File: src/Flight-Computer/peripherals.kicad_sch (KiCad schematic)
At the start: 0 parts

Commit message: implemented usb transceiver in schematic
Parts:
- added C16: 1uF, symbol Flight-Computer:CAP_0603
- added C17: 0.1uF, symbol Flight-Computer:CAP_0603
- added D6: SP0504BAHTG, SOD-123FL_MCC, symbol Flight-Computer:SP0504BAHTG
- added P3: USB, BEL_SS-52300-001, symbol Flight-Computer:USB
- added R3: 4.7k, symbol Flight-Computer:RES_0603
- added R5: 10k, symbol Flight-Computer:RES_0603
- added U3: CP2102-GMR(QFN28), QFN28G_0.5-5X5MM, symbol Flight-Computer:CP2102-GMR(QFN28)
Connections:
- new net 3.3V: R3.1
- new net 5V: C16.1, C17.1, D6.1, P3.1 (VCC), U3.7 (REGIN), U3.8 (VBUS)
- new net D+: D6.4, P3.3 (D+), U3.4 (D+)
- new net D-: D6.3, P3.2 (D-), U3.5 (D-)
- new net Earth: C16.2, C17.2, D6.2, P3.5 (GND), P3.S1 (SHIELD), P3.S2 (SHIELD), R5.1, U3.29 (PAD), U3.3 (GND)
- new net RX_USB: U3.25 (RXD)
- new net TX_USB: U3.26 (TXD)
- new net ~{USB_RST}: R3.2, U3.9 (~{RST})
- new net ~{USB_SUSPEND}: R5.2, U3.11 (~{SUSPEND})
- no-connect marks 0 -> 20
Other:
- note added: "USB Transceiver"

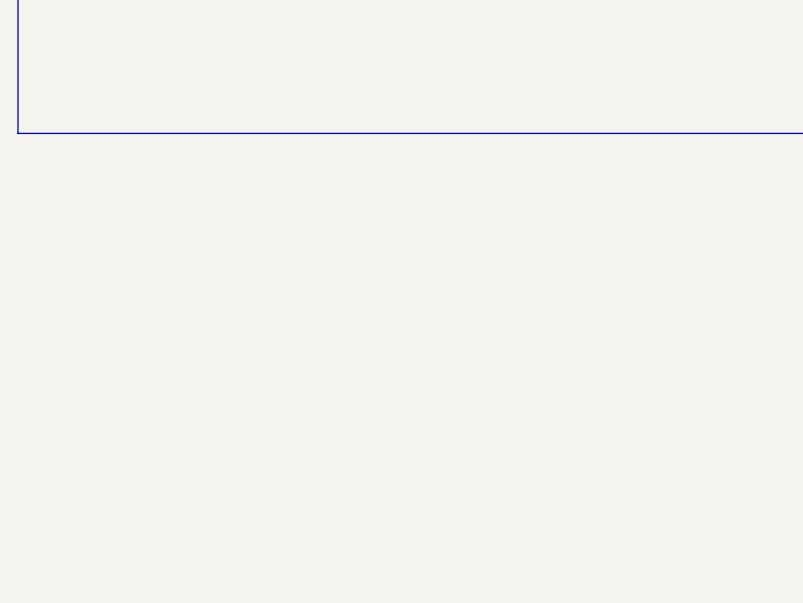
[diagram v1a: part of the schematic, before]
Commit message: implemented flash in schematic
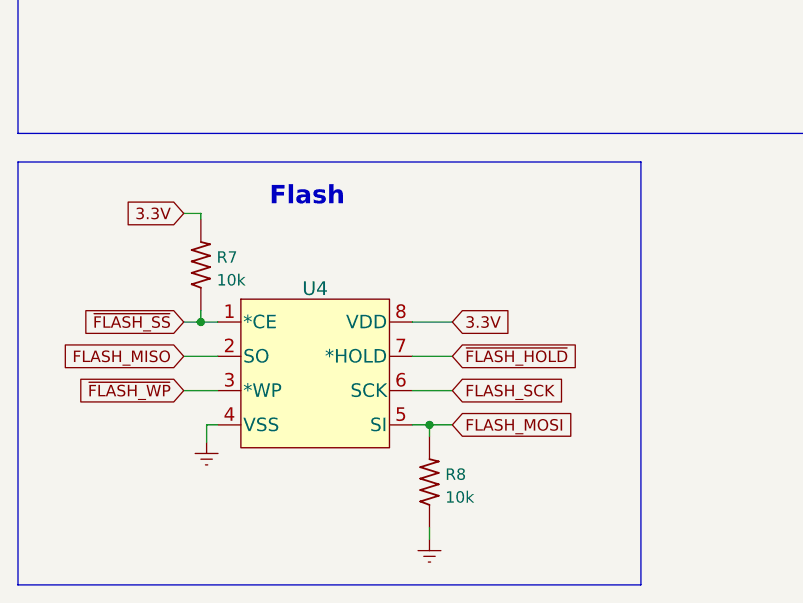
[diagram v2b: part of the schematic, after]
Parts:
- added R7, R8: 10k, symbol Flight-Computer:RES_0603
- added U4: SST25VF040B-50-4I-S2AE-T, SOIC8_S2A_SST_MCH, symbol Flight-Computer:SST25VF040B-50-4I-S2AE-T
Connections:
- net 3.3V: now also R7.2, U4.8 (VDD)
- net Earth: now also R8.1, U4.4 (VSS)
- new net FLASH_MISO: U4.2 (SO)
- new net FLASH_MOSI: R8.2, U4.5 (SI)
- new net FLASH_SCK: U4.6 (SCK)
- new net ~{FLASH_HOLD}: U4.7 (*HOLD)
- new net ~{FLASH_SS}: R7.1, U4.1 (*CE)
- new net ~{FLASH_WP}: U4.3 (*WP)
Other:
- note added: "Flash"

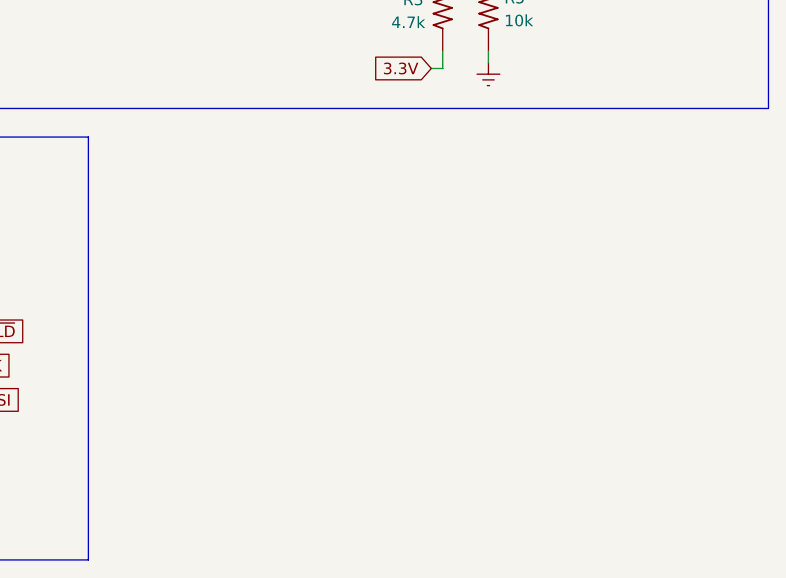
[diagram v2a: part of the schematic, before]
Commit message: added comparator to lib files
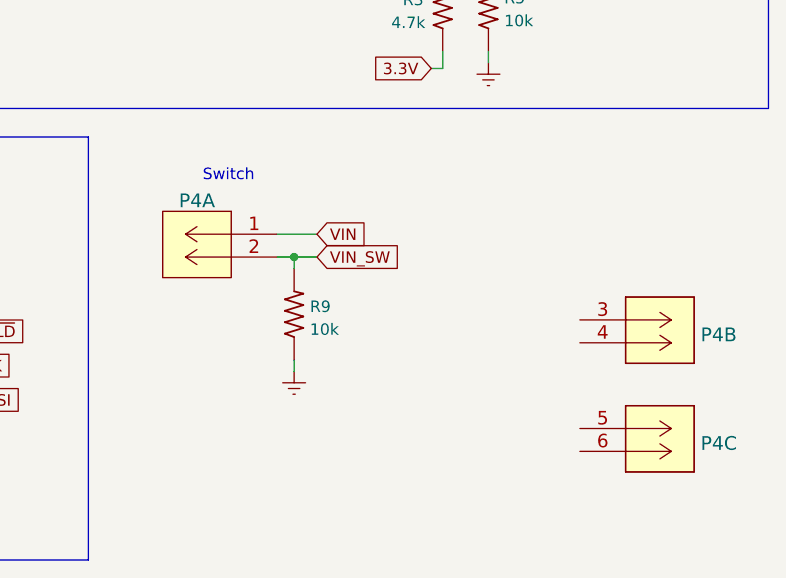
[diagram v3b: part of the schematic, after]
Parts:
- added P4: 282837-6, 66953-005LF_AMP, symbol Flight-Computer:282837-6
- added R9: 10k, symbol Flight-Computer:RES_0603
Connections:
- net Earth: now also R9.1
- new net VIN: P4.1 (5)
- new net VIN_SW: P4.2 (6), R9.2
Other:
- note added: "Switch"
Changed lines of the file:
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@@
   (junction (at 69.85 50.8) (diameter 0) (color 0 0 0 0)
+  )
+  (junction (at 109.855 107.95) (diameter 0) (color 0 0 0 0)
   )
   (junction (at 63.5 123.825) (diameter 0) (color 0 0 0 0)
@@
     (stroke (width 0) (type default) (color 0 0 0 0))
   )
+  (wire (pts (xy 107.95 107.95) (xy 109.855 107.95))
+    (stroke (width 0) (type default) (color 0 0 0 0))
+  )
   (wire (pts (xy 111.125 45.72) (xy 107.95 45.72))
     (stroke (width 0) (type default) (color 0 0 0 0))
@@
     (stroke (width 0) (type default) (color 0 0 0 0))
   )
+  (wire (pts (xy 109.855 107.95) (xy 112.395 107.95))
+    (stroke (width 0) (type default) (color 0 0 0 0))
+  )
   (wire (pts (xy 61.595 112.395) (xy 66.04 112.395))
     (stroke (width 0) (type default) (color 0 0 0 0))
@@
     (stroke (width 0) (type default) (color 0 0 0 0))
   )
+  (wire (pts (xy 109.855 107.95) (xy 109.855 109.22))
+    (stroke (width 0) (type default) (color 0 0 0 0))
+  )
   (wire (pts (xy 107.95 45.72) (xy 107.95 52.07))
     (stroke (width 0) (type default) (color 0 0 0 0))
@@
     (stroke (width 0) (type default) (color 0 0 0 0))
   )
+  (wire (pts (xy 109.855 119.38) (xy 109.855 120.65))
+    (stroke (width 0) (type default) (color 0 0 0 0))
+  )
   (polyline (pts (xy 17.78 18.415) (xy 17.78 91.44))
     (stroke (width 0) (type default) (color 0 0 0 0))
@@
     (stroke (width 0) (type default) (color 0 0 0 0))
   )
+  (wire (pts (xy 107.95 105.41) (xy 112.395 105.41))
+    (stroke (width 0) (type default) (color 0 0 0 0))
+  )
   (wire (pts (xy 61.595 123.825) (xy 63.5 123.825))
     (stroke (width 0) (type default) (color 0 0 0 0))
@@
   (wire (pts (xy 62.865 48.26) (xy 62.865 52.07))
     (stroke (width 0) (type default) (color 0 0 0 0))
+  )
+  (text "Switch" (at 99.695 99.695 0)
+    (effects (font (size 1.27 1.27)) (justify left bottom))
   )
   (text "Flash" (at 45.72 99.695 0)
@@
     )
   )
+  (global_label "VIN_SW" (shape input) (at 112.395 107.95 0) (fields_autoplaced)
+    (effects (font (size 1.27 1.27)) (justify left))
+    (property "Intersheet References" "${INTERSHEET_REFS}" (id 0) (at 121.3716 107.8706 0)
+      (effects (font (size 1.27 1.27)) (justify left) hide)
+    )
+  )
   (global_label "5V" (shape input) (at 121.285 69.215 180) (fields_autoplaced)
     (effects (font (size 1.27 1.27)) (justify right))
@@
     )
   )
+  (global_label "VIN" (shape input) (at 112.395 105.41 0) (fields_autoplaced)
+    (effects (font (size 1.27 1.27)) (justify left))
+    (property "Intersheet References" "${INTERSHEET_REFS}" (id 0) (at 117.743 105.3306 0)
+      (effects (font (size 1.27 1.27)) (justify left) hide)
+    )
+  )
   (global_label "3.3V" (shape input) (at 125.095 86.995 180) (fields_autoplaced)
     (effects (font (size 1.27 1.27)) (justify right))
@@
     )
   )
+  (symbol (lib_id "Flight-Computer:282837-6") (at 107.95 105.41 0) (mirror y) (unit 1)
+    (in_bom yes) (on_board yes) (fields_autoplaced)
+    (property "Reference" "P4" (id 0) (at 99.06 101.7031 0)
+      (effects (font (size 1.524 1.524)))
+    )
+    (property "Value" "282837-6" (id 1) (at 102.87 133.35 0)
+      (effects (font (size 1.524 1.524)) hide)
+    )
+    (property "Footprint" "66953-005LF_AMP" (id 2) (at 104.14 135.89 0)
+      (effects (font (size 1.524 1.524)) hide)
+    )
+    (property "Datasheet" "" (id 3) (at 107.95 105.41 0)
+      (effects (font (size 1.524 1.524)) hide)
+    )
+    (pin "1")
+    (pin "2")
+    (pin "3")
+    (pin "4")
+    (pin "5")
+    (pin "6")
+  )
   (symbol (lib_id "Flight-Computer:CAP_0603") (at 100.33 60.96 90) (unit 1)
     (in_bom yes) (on_board yes) (fields_autoplaced)
@@
     )
     (pin "1")
+  )
+  (symbol (lib_id "Flight-Computer:282837-6") (at 141.605 114.935 0) (unit 2)
+    (in_bom yes) (on_board yes) (fields_autoplaced)
+    (property "Reference" "P4" (id 0) (at 155.0162 116.5985 0)
+      (effects (font (size 1.524 1.524)) (justify left))
+    )
+    (property "Value" "282837-6" (id 1) (at 146.685 142.875 0)
+      (effects (font (size 1.524 1.524)) hide)
+    )
+    (property "Footprint" "66953-005LF_AMP" (id 2) (at 145.415 145.415 0)
+      (effects (font (size 1.524 1.524)) hide)
+    )
+    (property "Datasheet" "" (id 3) (at 141.605 114.935 0)
+      (effects (font (size 1.524 1.524)) hide)
+    )
+    (pin "1")
+    (pin "2")
+    (pin "3")
+    (pin "4")
+    (pin "5")
+    (pin "6")
+  )
+  (symbol (lib_id "Flight-Computer:RES_0603") (at 109.855 114.3 90) (unit 1)
+    (in_bom yes) (on_board yes) (fields_autoplaced)
+    (property "Reference" "R9" (id 0) (at 111.6076 113.4653 90)
+      (effects (font (size 1.27 1.27)) (justify right))
+    )
+    (property "Value" "10k" (id 1) (at 111.6076 116.0022 90)
+      (effects (font (size 1.27 1.27)) (justify right))
+    )
+    (property "Footprint" "" (id 2) (at 122.555 113.03 0)
+      (effects (font (size 1.27 1.27)) (justify left bottom) hide)
+    )
+    (property "Datasheet" "" (id 3) (at 109.855 114.3 0)
+      (effects (font (size 1.27 1.27)) (justify left bottom) hide)
+    )
+    (pin "1")
+    (pin "2")
   )
   (symbol (lib_id "Flight-Computer:SST25VF040B-50-4I-S2AE-T") (at 51.435 114.935 0) (unit 1)
@@
     (pin "7")
     (pin "8")
+  )
+  (symbol (lib_id "Flight-Computer:Earth") (at 109.855 120.65 0) (unit 1)
+    (in_bom yes) (on_board yes) (fields_autoplaced)
+    (property "Reference" "#PWR022" (id 0) (at 109.855 127 0)
+      (effects (font (size 1.27 1.27)) hide)
+    )
+    (property "Value" "Earth" (id 1) (at 109.855 124.46 0)
+      (effects (font (size 1.27 1.27)) hide)
+    )
+    (property "Footprint" "" (id 2) (at 109.855 120.65 0)
+      (effects (font (size 1.27 1.27)) hide)
+    )
+    (property "Datasheet" "" (id 3) (at 109.855 120.65 0)
+      (effects (font (size 1.27 1.27)) hide)
+    )
+    (pin "1")
   )
   (symbol (lib_id "Flight-Computer:RES_0603") (at 126.365 80.01 90) (unit 1)
@@
     (pin "1")
   )
+  (symbol (lib_id "Flight-Computer:282837-6") (at 141.605 127 0) (unit 3)
+    (in_bom yes) (on_board yes) (fields_autoplaced)
+    (property "Reference" "P4" (id 0) (at 155.0162 128.6635 0)
+      (effects (font (size 1.524 1.524)) (justify left))
+    )
+    (property "Value" "282837-6" (id 1) (at 146.685 154.94 0)
+      (effects (font (size 1.524 1.524)) hide)
+    )
+    (property "Footprint" "66953-005LF_AMP" (id 2) (at 145.415 157.48 0)
+      (effects (font (size 1.524 1.524)) hide)
+    )
+    (property "Datasheet" "" (id 3) (at 141.605 127 0)
+      (effects (font (size 1.524 1.524)) hide)
+    )
+    (pin "1")
+    (pin "2")
+    (pin "3")
+    (pin "4")
+    (pin "5")
+    (pin "6")
+  )
   (symbol (lib_id "Flight-Computer:RES_0603") (at 38.1 106.045 90) (unit 1)
